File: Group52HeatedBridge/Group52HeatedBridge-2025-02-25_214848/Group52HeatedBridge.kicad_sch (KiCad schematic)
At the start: 2 parts

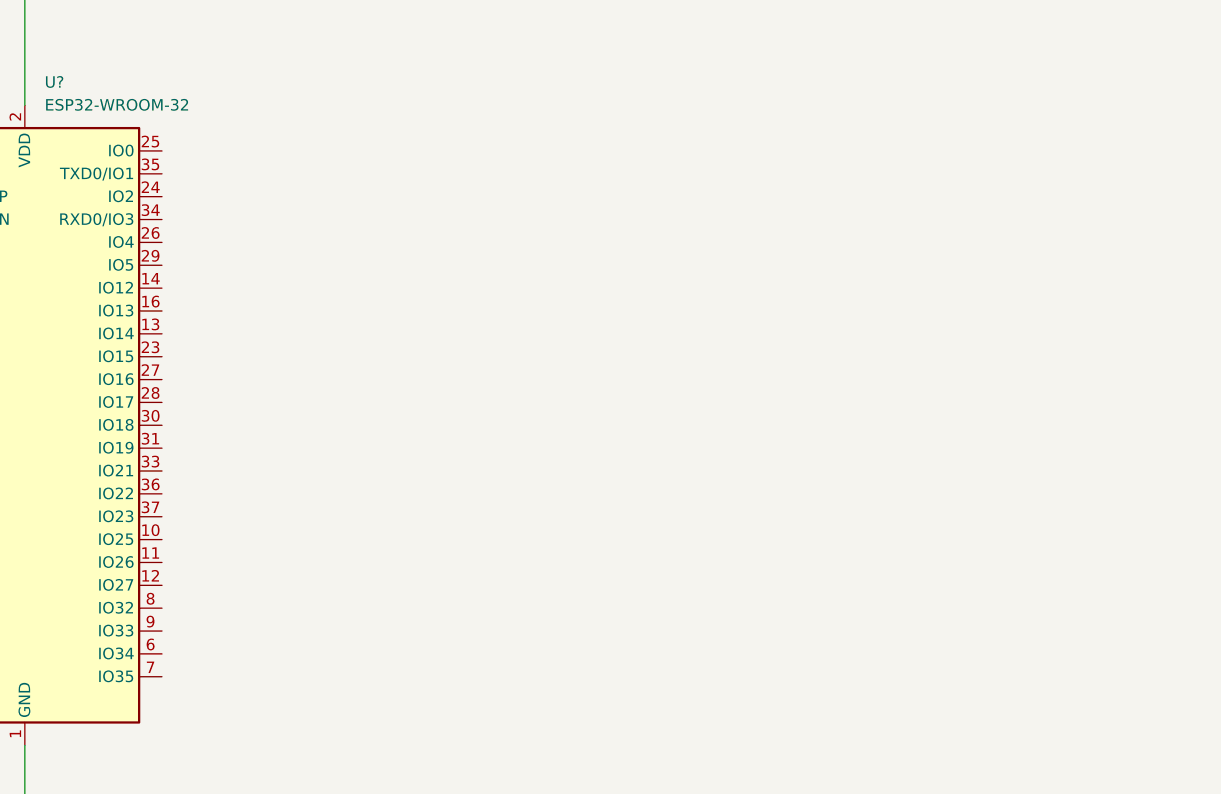
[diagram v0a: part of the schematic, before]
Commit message: added connectors and researched new temp sensor that is waterproof and easy to interface with
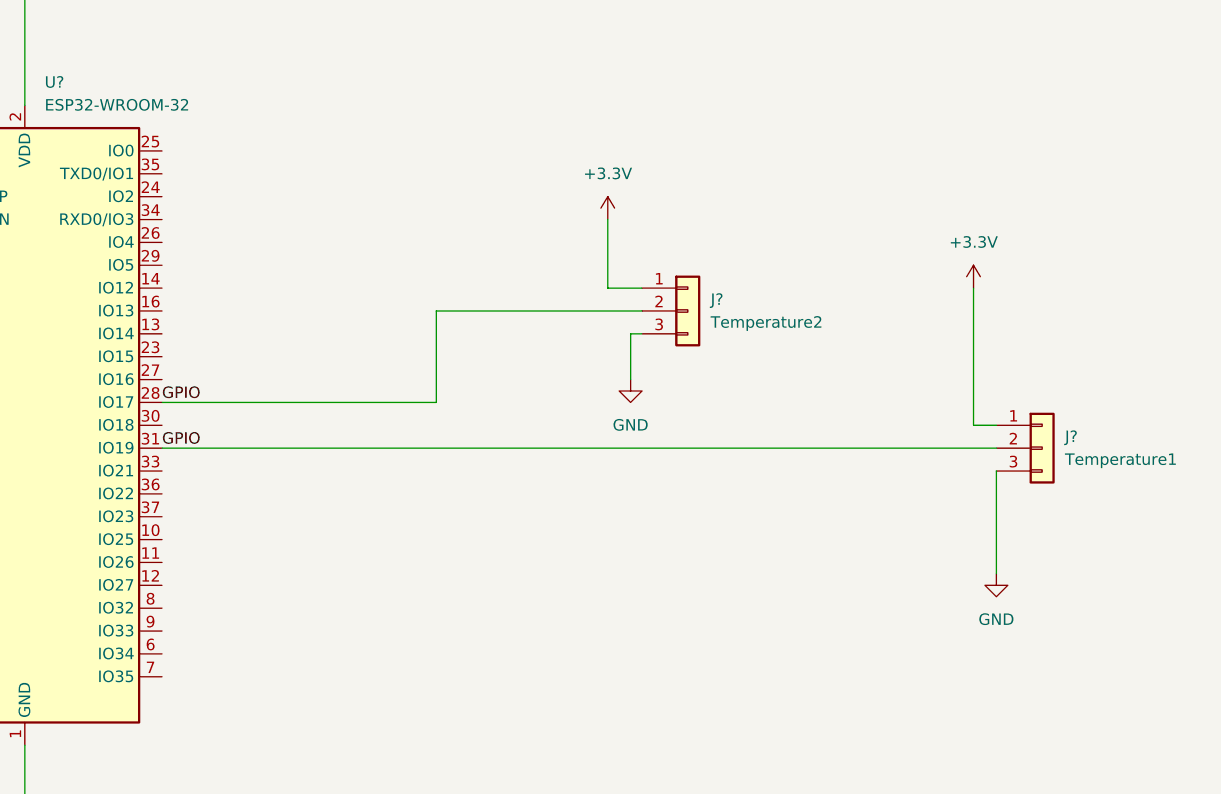
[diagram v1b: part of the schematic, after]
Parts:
- added J?: Temperature2, symbol Connector_Generic:Conn_01x03
- added J?: Temperature1, symbol Connector_Generic:Conn_01x03
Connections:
- net +3.3V: now also J?.1 (Pin_1), J?.1 (Pin_1)
- net GND: now also J?.3 (Pin_3), J?.3 (Pin_3)
- net GPIO: now reaches U?.28 (IO17)
- net GPIO: now also U?.31 (IO19), J?.2 (Pin_2), J?.2 (Pin_2)
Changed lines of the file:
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@@
   (junction (at 130.81 45.72) (diameter 0) (color 0 0 0 0)
   )
+  (wire (pts (xy 199.39 85.09) (xy 198.12 85.09))
+    (stroke (width 0) (type default))
+  )
   (wire (pts (xy 93.98 49.53) (xy 93.98 45.72))
     (stroke (width 0) (type default))
   )
+  (wire (pts (xy 198.12 85.09) (xy 198.12 90.17))
+    (stroke (width 0) (type default))
+  )
+  (wire (pts (xy 238.76 100.33) (xy 238.76 111.76))
+    (stroke (width 0) (type default))
+  )
   (wire (pts (xy 130.81 130.81) (xy 130.81 140.97))
     (stroke (width 0) (type default))
@@
     (stroke (width 0) (type default))
   )
+  (wire (pts (xy 146.05 97.79) (xy 238.76 97.79))
+    (stroke (width 0) (type default))
+  )
+  (wire (pts (xy 199.39 80.01) (xy 195.58 80.01))
+    (stroke (width 0) (type default))
+  )
   (wire (pts (xy 104.14 45.72) (xy 130.81 45.72))
     (stroke (width 0) (type default))
   )
+  (wire (pts (xy 176.53 92.71) (xy 176.53 82.55))
+    (stroke (width 0) (type default))
+  )
+  (wire (pts (xy 176.53 82.55) (xy 199.39 82.55))
+    (stroke (width 0) (type default))
+  )
+  (wire (pts (xy 238.76 95.25) (xy 236.22 95.25))
+    (stroke (width 0) (type default))
+  )
+  (wire (pts (xy 195.58 80.01) (xy 195.58 72.39))
+    (stroke (width 0) (type default))
+  )
+  (wire (pts (xy 146.05 92.71) (xy 176.53 92.71))
+    (stroke (width 0) (type default))
+  )
   (wire (pts (xy 130.81 45.72) (xy 130.81 59.69))
     (stroke (width 0) (type default))
   )
+  (wire (pts (xy 236.22 95.25) (xy 236.22 80.01))
+    (stroke (width 0) (type default))
+  )
+  (label "GPIO" (at 146.05 97.79 0) (fields_autoplaced)
+    (effects (font (size 1.27 1.27)) (justify left bottom))
+  )
+  (label "GPIO" (at 146.05 92.71 0) (fields_autoplaced)
+    (effects (font (size 1.27 1.27)) (justify left bottom))
+  )
+  (symbol (lib_id "power:+3.3V") (at 236.22 80.01 0) (unit 1)
+    (in_bom yes) (on_board yes) (dnp no) (fields_autoplaced)
+    (property "Reference" "#PWR05" (at 236.22 83.82 0)
+      (effects (font (size 1.27 1.27)) hide)
+    )
+    (property "Value" "+3.3V" (at 236.22 74.93 0)
+      (effects (font (size 1.27 1.27)))
+    )
+    (property "Footprint" "" (at 236.22 80.01 0)
+      (effects (font (size 1.27 1.27)) hide)
+    )
+    (property "Datasheet" "" (at 236.22 80.01 0)
+      (effects (font (size 1.27 1.27)) hide)
+    )
+    (pin "1")
+    (instances
+      (project "Group52HeatedBridge"
+        (path "/bb48adda-4915-4436-95dc-e9dcb2cba51b"
+          (reference "#PWR05") (unit 1)
+        )
+      )
+    )
+  )
+  (symbol (lib_id "power:GND") (at 238.76 111.76 0) (unit 1)
+    (in_bom yes) (on_board yes) (dnp no) (fields_autoplaced)
+    (property "Reference" "#PWR07" (at 238.76 118.11 0)
+      (effects (font (size 1.27 1.27)) hide)
+    )
+    (property "Value" "GND" (at 238.76 116.84 0)
+      (effects (font (size 1.27 1.27)))
+    )
+    (property "Footprint" "" (at 238.76 111.76 0)
+      (effects (font (size 1.27 1.27)) hide)
+    )
+    (property "Datasheet" "" (at 238.76 111.76 0)
+      (effects (font (size 1.27 1.27)) hide)
+    )
+    (pin "1")
+    (instances
+      (project "Group52HeatedBridge"
+        (path "/bb48adda-4915-4436-95dc-e9dcb2cba51b"
+          (reference "#PWR07") (unit 1)
+        )
+      )
+    )
+  )
   (symbol (lib_id "power:GND") (at 130.81 140.97 0) (unit 1)
     (in_bom yes) (on_board yes) (dnp no) (fields_autoplaced)
@@
         (path "/bb48adda-4915-4436-95dc-e9dcb2cba51b"
           (reference "C1") (unit 1)
+        )
+      )
+    )
+  )
+  (symbol (lib_id "power:GND") (at 198.12 90.17 0) (unit 1)
+    (in_bom yes) (on_board yes) (dnp no) (fields_autoplaced)
+    (property "Reference" "#PWR06" (at 198.12 96.52 0)
+      (effects (font (size 1.27 1.27)) hide)
+    )
+    (property "Value" "GND" (at 198.12 95.25 0)
+      (effects (font (size 1.27 1.27)))
+    )
+    (property "Footprint" "" (at 198.12 90.17 0)
+      (effects (font (size 1.27 1.27)) hide)
+    )
+    (property "Datasheet" "" (at 198.12 90.17 0)
+      (effects (font (size 1.27 1.27)) hide)
+    )
+    (pin "1")
+    (instances
+      (project "Group52HeatedBridge"
+        (path "/bb48adda-4915-4436-95dc-e9dcb2cba51b"
+          (reference "#PWR06") (unit 1)
         )
       )
@@
     )
   )
+  (symbol (lib_id "power:+3.3V") (at 195.58 72.39 0) (unit 1)
+    (in_bom yes) (on_board yes) (dnp no) (fields_autoplaced)
+    (property "Reference" "#PWR04" (at 195.58 76.2 0)
+      (effects (font (size 1.27 1.27)) hide)
+    )
+    (property "Value" "+3.3V" (at 195.58 67.31 0)
+      (effects (font (size 1.27 1.27)))
+    )
+    (property "Footprint" "" (at 195.58 72.39 0)
+      (effects (font (size 1.27 1.27)) hide)
+    )
+    (property "Datasheet" "" (at 195.58 72.39 0)
+      (effects (font (size 1.27 1.27)) hide)
+    )
+    (pin "1")
+    (instances
+      (project "Group52HeatedBridge"
+        (path "/bb48adda-4915-4436-95dc-e9dcb2cba51b"
+          (reference "#PWR04") (unit 1)
+        )
+      )
+    )
+  )
   (symbol (lib_id "power:GND") (at 93.98 49.53 0) (unit 1)
     (in_bom yes) (on_board yes) (dnp no) (fields_autoplaced)
@@
         )
       )
+    )
+  )
+  (symbol (lib_id "Connector_Generic:Conn_01x03") (at 204.47 82.55 0) (unit 1)
+    (in_bom yes) (on_board yes) (dnp no) (fields_autoplaced)
+    (property "Reference" "J?" (at 207.01 81.28 0)
+      (effects (font (size 1.27 1.27)) (justify left))
+    )
+    (property "Value" "Temperature2" (at 207.01 83.82 0)
+      (effects (font (size 1.27 1.27)) (justify left))
+    )
+    (property "Footprint" "" (at 204.47 82.55 0)
+      (effects (font (size 1.27 1.27)) hide)
+    )
+    (property "Datasheet" "~" (at 204.47 82.55 0)
+      (effects (font (size 1.27 1.27)) hide)
+    )
+    (pin "1")
+    (pin "2")
+    (pin "3")
+    (instances
+      (project "Group52HeatedBridge"
+        (path "/bb48adda-4915-4436-95dc-e9dcb2cba51b"
+          (reference "J?") (unit 1)
+        )
+      )
+    )
+  )
+  (symbol (lib_id "Connector_Generic:Conn_01x03") (at 243.84 97.79 0) (unit 1)
+    (in_bom yes) (on_board yes) (dnp no) (fields_autoplaced)
+    (property "Reference" "J?" (at 246.38 96.52 0)
+      (effects (font (size 1.27 1.27)) (justify left))
+    )
+    (property "Value" "Temperature1" (at 246.38 99.06 0)
+      (effects (font (size 1.27 1.27)) (justify left))
+    )
+    (property "Footprint" "" (at 243.84 97.79 0)
+      (effects (font (size 1.27 1.27)) hide)
+    )
+    (property "Datasheet" "~" (at 243.84 97.79 0)
+      (effects (font (size 1.27 1.27)) hide)
+    )
+    (pin "1")
+    (pin "2")
+    (pin "3")
+    (instances
+      (project "Group52HeatedBridge"
+        (path "/bb48adda-4915-4436-95dc-e9dcb2cba51b"
+          (reference "J?") (unit 1)
+        )
+      )

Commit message: updated schematic
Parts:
- added C? (x2): 1uF, symbol Device:C
- added J?: UART, symbol Connector_Generic:Conn_01x03
- added R? (x2): 10k, symbol Device:R
- added SW?: BOOT_BUTTON, symbol Switch:SW_Push
- added SW?: EN_BUTTON, symbol Switch:SW_Push
- J?: value Temperature2 -> TemperatureSurface
- J?: value Temperature1 -> TemperatureAir
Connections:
- net +3.3V: now also C1.1, R?.2, R?.2; no longer C1.2
- net GND: now also C1.2, C?.1, C?.2, J?.3 (Pin_3), SW?.1, SW?.2; no longer C1.1
- net at U?.25 (IO0): now also C?.1, R?.1, SW?.1
- net at U?.3 (EN): now also C?.2, R?.1, SW?.2
- net RX: now reaches U?.34 (RXD0/IO3)
- net RX: now also J?.2 (Pin_2)
- net TX: now reaches U?.35 (TXD0/IO1)
- net TX: now also J?.1 (Pin_1)
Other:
- moved on the sheet: C1, J?, U?

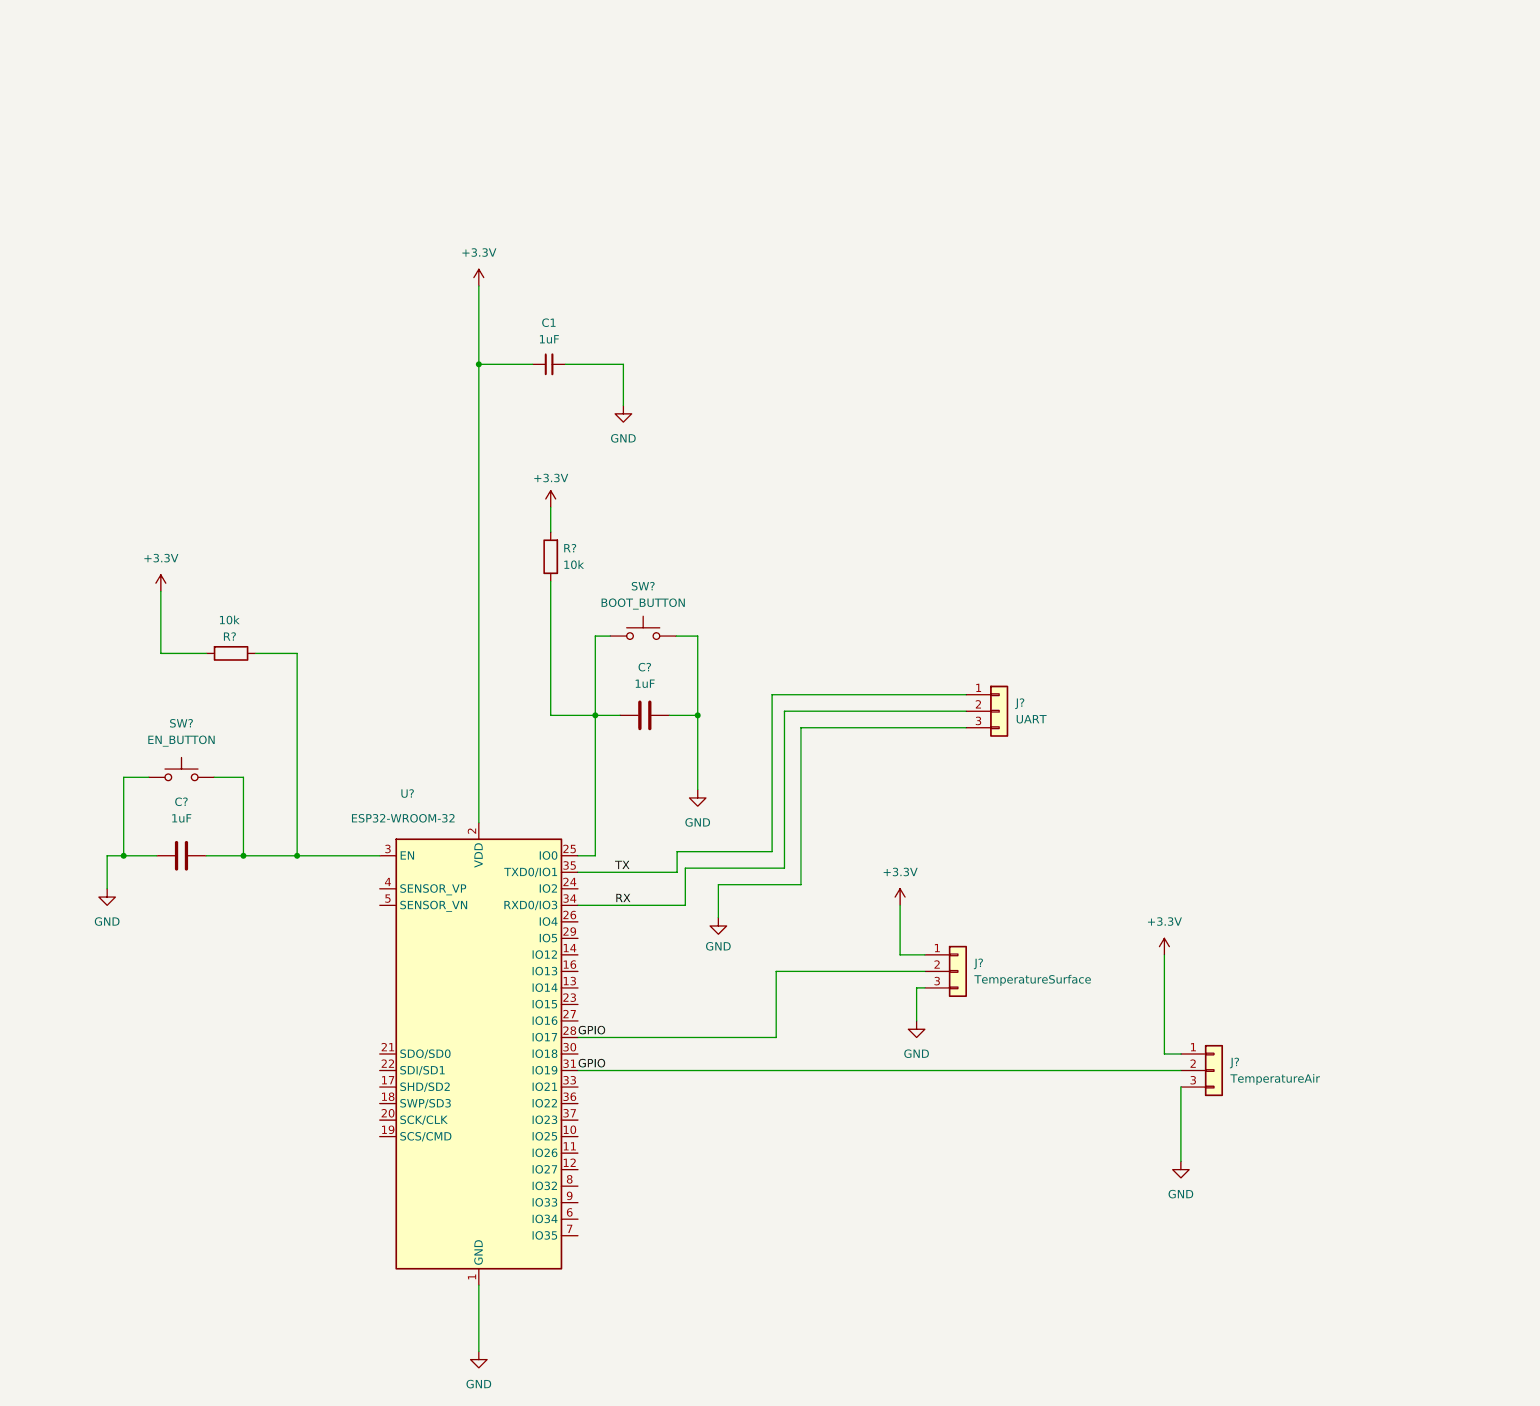
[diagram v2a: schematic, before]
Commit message: grid size update fix
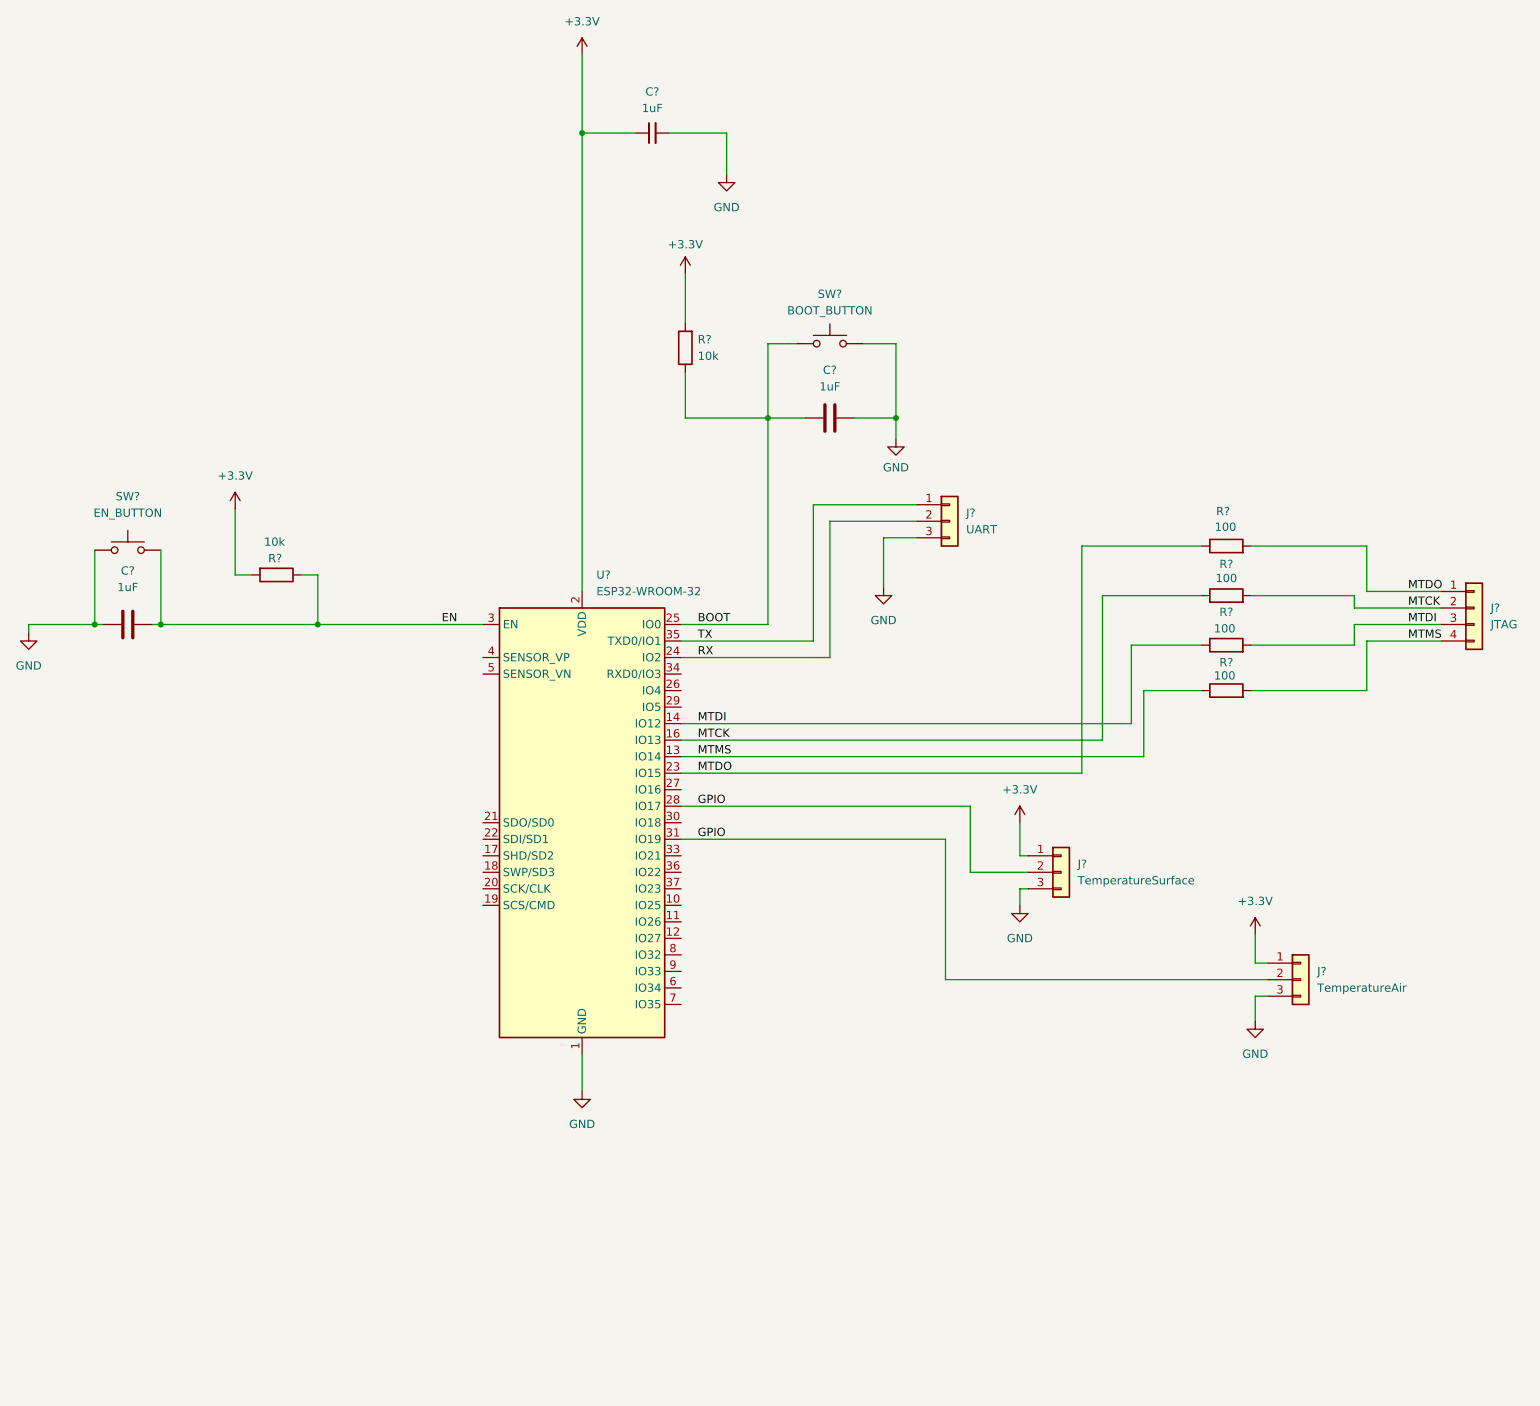
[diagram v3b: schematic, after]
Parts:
- removed C1: 1uF, symbol Device:C_Small
- removed R?: 10k, symbol Device:R
- removed U?: ESP32-WROOM-32, RF_Module:ESP32-WROOM-32, symbol RF_Module:ESP32-WROOM-32
- added C?: 1uF, symbol Device:C_Small
- added J?: JTAG, symbol Connector_Generic:Conn_01x04
- added R? (x4): 100, symbol Device:R
- added R?: 10k, symbol Device:R
- added U?: ESP32-WROOM-32, RF_Module:ESP32-WROOM-32, symbol RF_Module:ESP32-WROOM-32
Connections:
- net +3.3V: now also C?.1, R?.2, U?.2 (VDD)
- net GND: now also C?.2, U?.1 (GND), U?.15 (GND), U?.38 (GND), U?.39 (GND)
- net GPIO: now also U?.28 (IO17), U?.31 (IO19)
- net RX: now also U?.24 (IO2)
- net TX: now also U?.35 (TXD0/IO1)
- net EN: now reaches C?.2, SW?.2
- net EN: now also R?.1, U?.3 (EN)
- net BOOT: now reaches C?.1, R?.1, SW?.1
- net BOOT: now also U?.25 (IO0)
- new net MTCK: J?.2 (Pin_2), R?.1, R?.2, U?.16 (IO13)
- new net MTDI: J?.3 (Pin_3), R?.1, R?.2, U?.14 (IO12)
- new net MTDO: J?.1 (Pin_1), R?.1, R?.2, U?.23 (IO15)
- new net MTMS: J?.4 (Pin_4), R?.1, R?.2, U?.13 (IO14)
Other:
- moved on the sheet: C?, J?, R?, SW?

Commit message: added footprints for barell jack
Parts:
- added J1: CON-SOCJ-2155, CON-SOCJ-2155:GRAVITECH_CON-SOCJ-2155, symbol CON-SOCJ-2155:CON-SOCJ-2155
- added J2: 54-00166, CONN3_54-00166_TEN, symbol 2025-02-28_21-13-51:54-00166
